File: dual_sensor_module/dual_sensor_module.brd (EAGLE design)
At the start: 27 x 39.4 mm, 14 parts, among them IC1 MCP602SN, IC2 TC7660DIL8

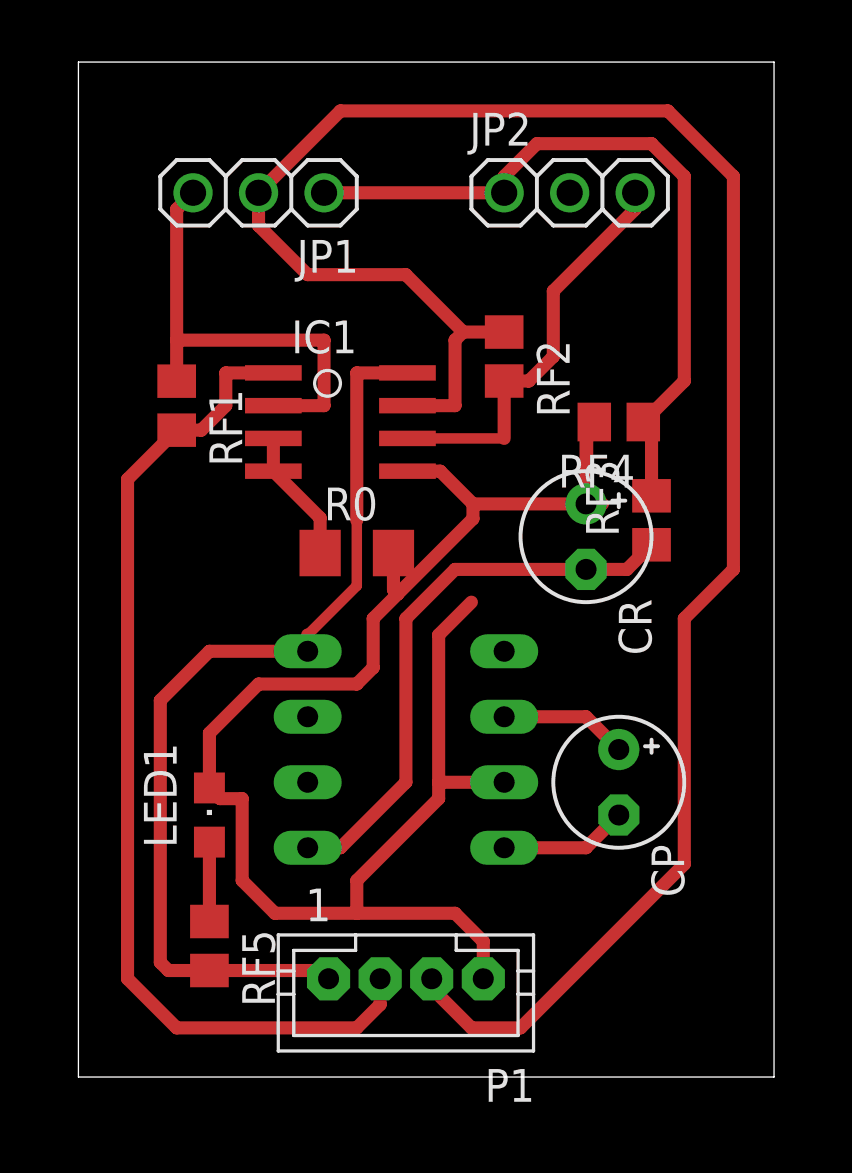
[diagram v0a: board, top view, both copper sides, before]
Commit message: agregado plano de tierra y modificadas las imagenes para corte
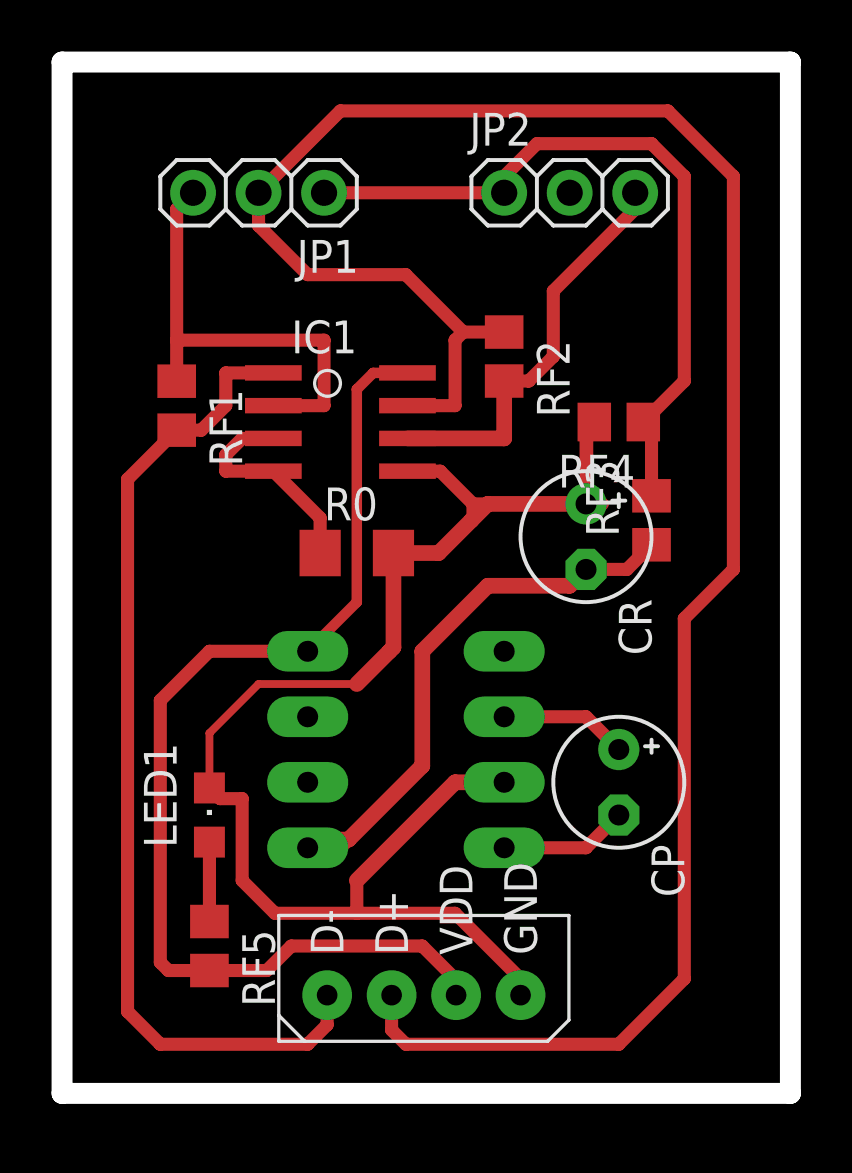
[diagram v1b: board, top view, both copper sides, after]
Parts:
- removed P1: (no value), jst-ph:JST-PH4
- added U$1: DYNAMIXEL_RS485, robot-hand:DYNAMIXEL_SPOX_04
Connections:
- net +5V: now also U$1.2; no longer P1.1
- net GND: now also U$1.1; no longer P1.4
- net VOUT1: now also U$1.4; no longer P1.2
- net VOUT2: now also U$1.3; no longer P1.3
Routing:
- net +5V: track 37.0 -> 43.0 mm
- net VOUT2: track 79.0 -> 84.0 mm
- net GND: track 71.4 -> 73.5 mm
- net VOUT1: track 39.4 -> 38.5 mm
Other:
- board size 27 x 39.4 mm -> 28.2 x 40 mm
